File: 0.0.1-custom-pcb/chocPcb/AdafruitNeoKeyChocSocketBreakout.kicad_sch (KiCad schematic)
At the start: 5 parts, among them J1 HC-FPC-0.5-6P-FH20, SW1 MX SOCKET

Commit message: choc rev1 looking good!
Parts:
- C1: value 1uF -> 100nF; footprint AdafruitNeoKeyChocSocketBreakout:0603-NO -> ProjectParts:C_0402_1005Metric; symbol AdafruitNeoKeyChocSocketBreakout-eagle-import:CAP_CERAMIC0603_NO -> ProjectParts:C_0402_Decoupling; MPN (none) -> GRM155R71C104JA88D; Manufacturer (none) -> Murata; Substitution (none) -> Compatible replacement; exact Glove80 BOM not verified
- LED1: value WS2812B_SK6812E -> WS2812B-2020; footprint AdafruitNeoKeyChocSocketBreakout:NEO3535_REVERSE -> ProjectParts:LED_WS2812B-2020_PLCC4_2.0x2.0mm; symbol AdafruitNeoKeyChocSocketBreakout-eagle-import:WS2812B_SK6812E -> ProjectParts:WS2812B-2020; MPN (none) -> WS2812B-2020; Manufacturer (none) -> Worldsemi; Substitution (none) -> Compatible replacement; exact Glove80 BOM not verified
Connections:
- net GND: now also LED1.2 (VSS); no longer LED1.3-GND (GND)
- net NEO_IN: now also LED1.3 (DIN); no longer LED1.4-DIN (DI)
- net NEO_OUT: now also LED1.1 (DOUT); no longer LED1.2-DOUT (DO)
- net VDD: now also LED1.4 (VDD); no longer LED1.1-VDD (VDD)

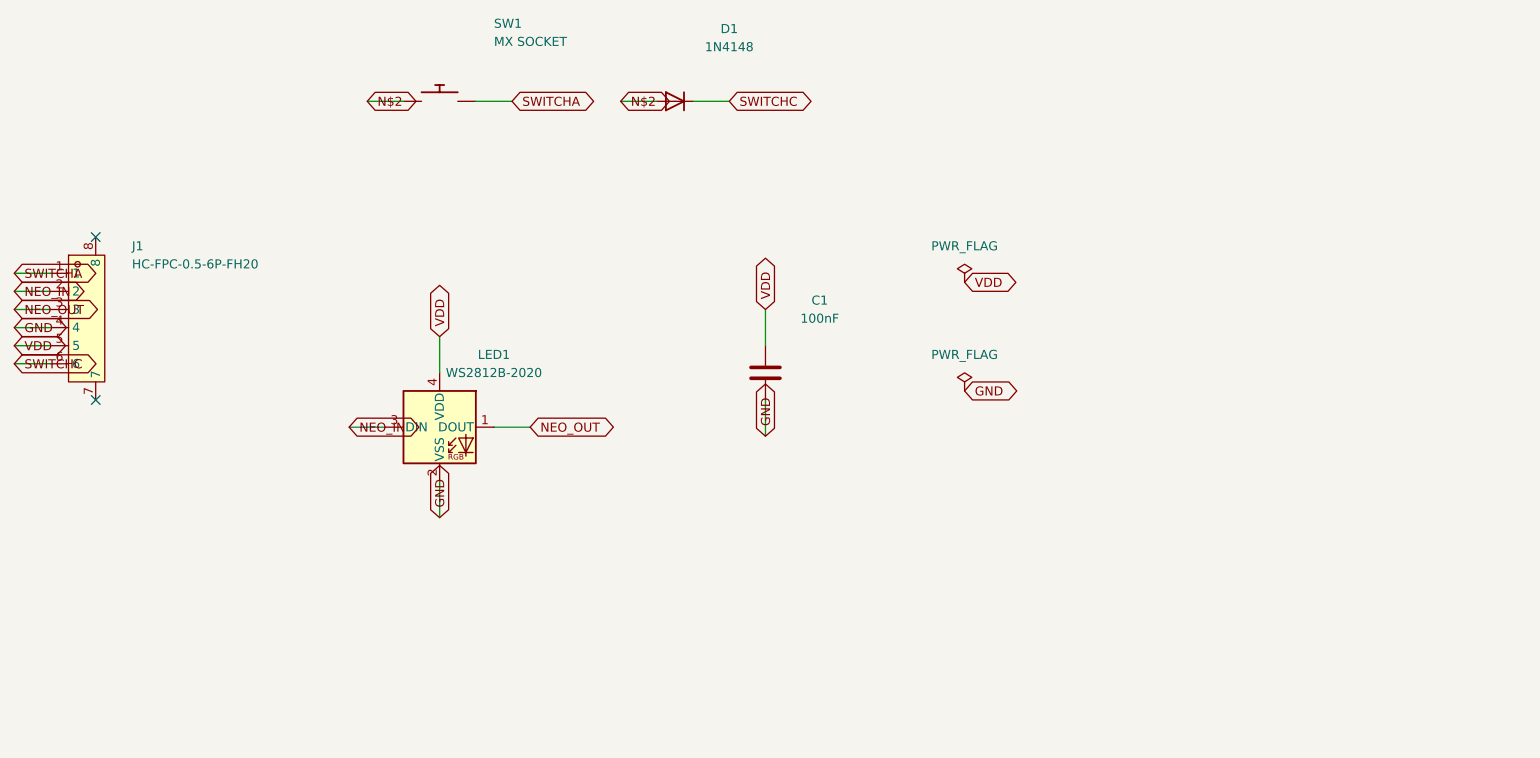
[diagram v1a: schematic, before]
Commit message: shorten ground line, clean up schematic
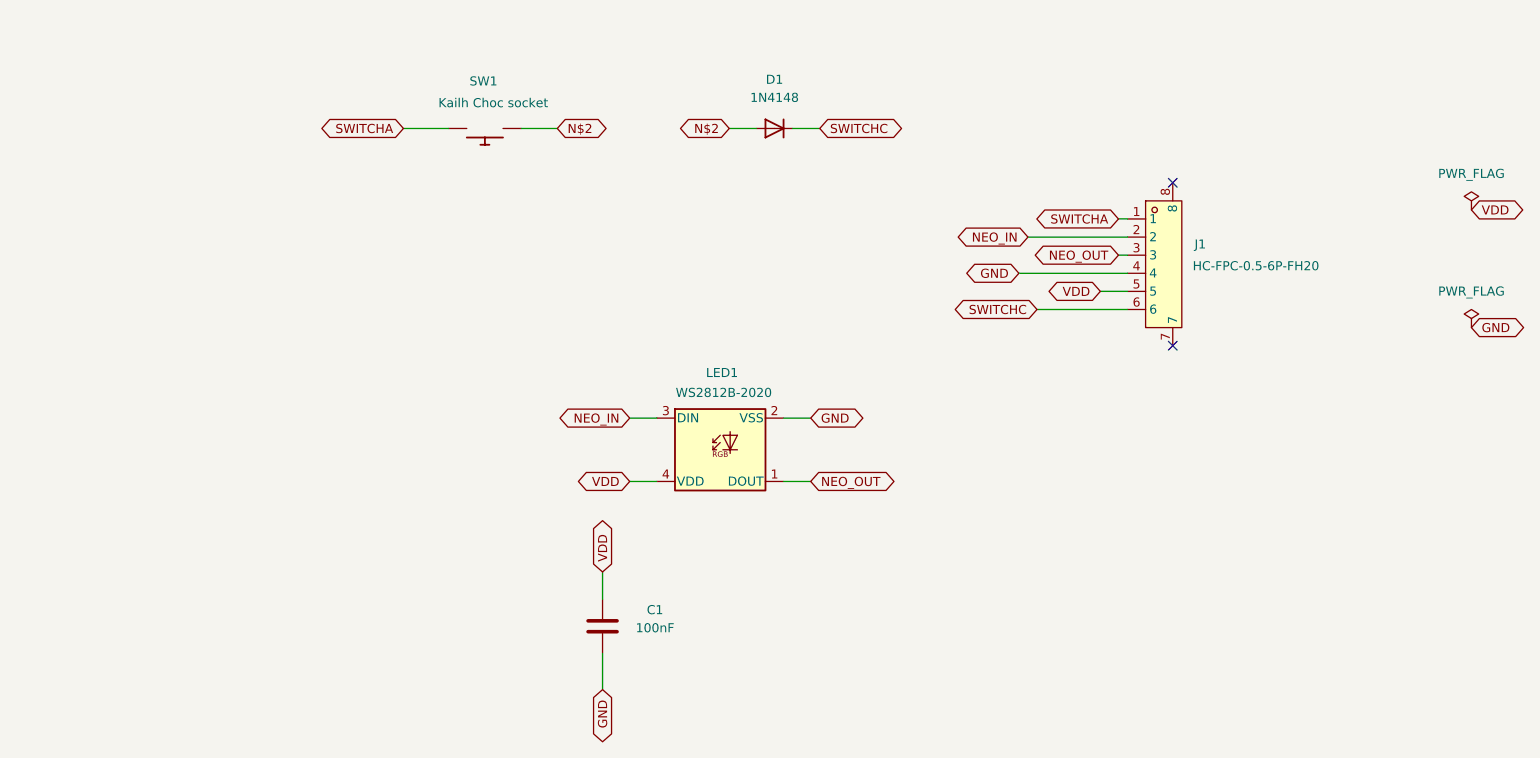
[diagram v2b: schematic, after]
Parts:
- SW1: value MX SOCKET -> Kailh Choc socket; MPN (none) -> CPG135001S30; Manufacturer (none) -> Kailh
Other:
- moved on the sheet: C1, D1, J1, LED1, SW1

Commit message: final changes to columnBreakout
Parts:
- C1: Dielectric (none) -> X7R; LCSC Part (none) -> C71629; MPN GRM155R71C104JA88D -> GRM155R71C104KA88D; Substitution Compatible replacement; exact Glove80 BOM not verified -> Equivalent 100nF 16V X7R 0402; 10% tolerance, JLC C71629; Tolerance (none) -> 10%; Voltage (none) -> 16V
- D1: value 1N4148 -> 1N4148WS; LCSC Part (none) -> C2128; MPN (none) -> 1N4148WS; Manufacturer (none) -> Jiangsu Changjing Electronics Technology Co., Ltd.
- J1: Manufacturer HC(虹成电子) -> Hong Cheng
- LED1: LCSC Part (none) -> C965555
- SW1: LCSC Part (none) -> C5333465
